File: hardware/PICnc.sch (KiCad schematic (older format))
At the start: 30 parts, among them P1 CONN_13X2, P2 CONN_5X2, P3 CONN_10X2, P4 CONN_8X2, P5 ICSP, P6 CONN_4X2, P7 CONN_2, P8 CONN_2, U1 PIC32MX764F128H, U2 LP2985LV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

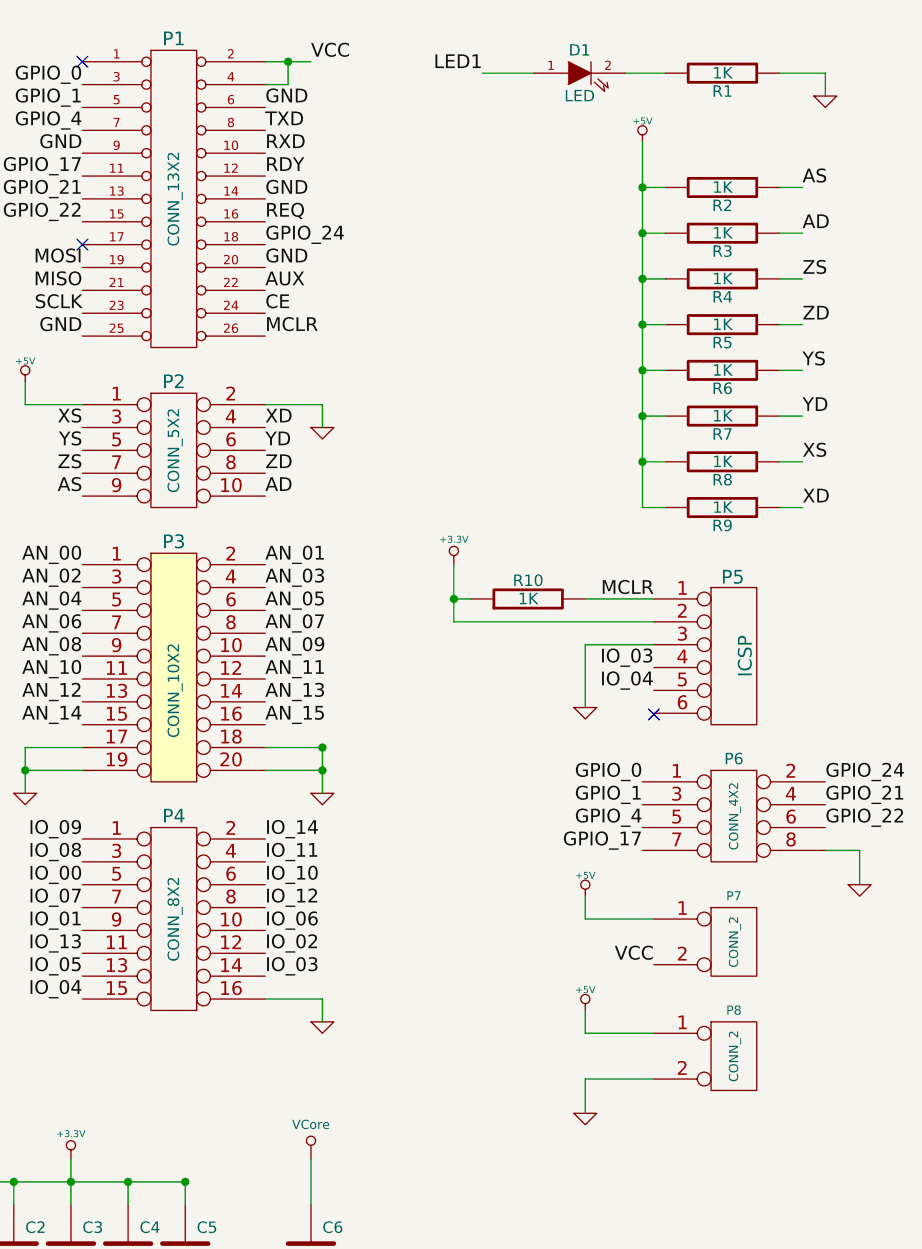
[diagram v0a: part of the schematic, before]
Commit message: minor schematic rename
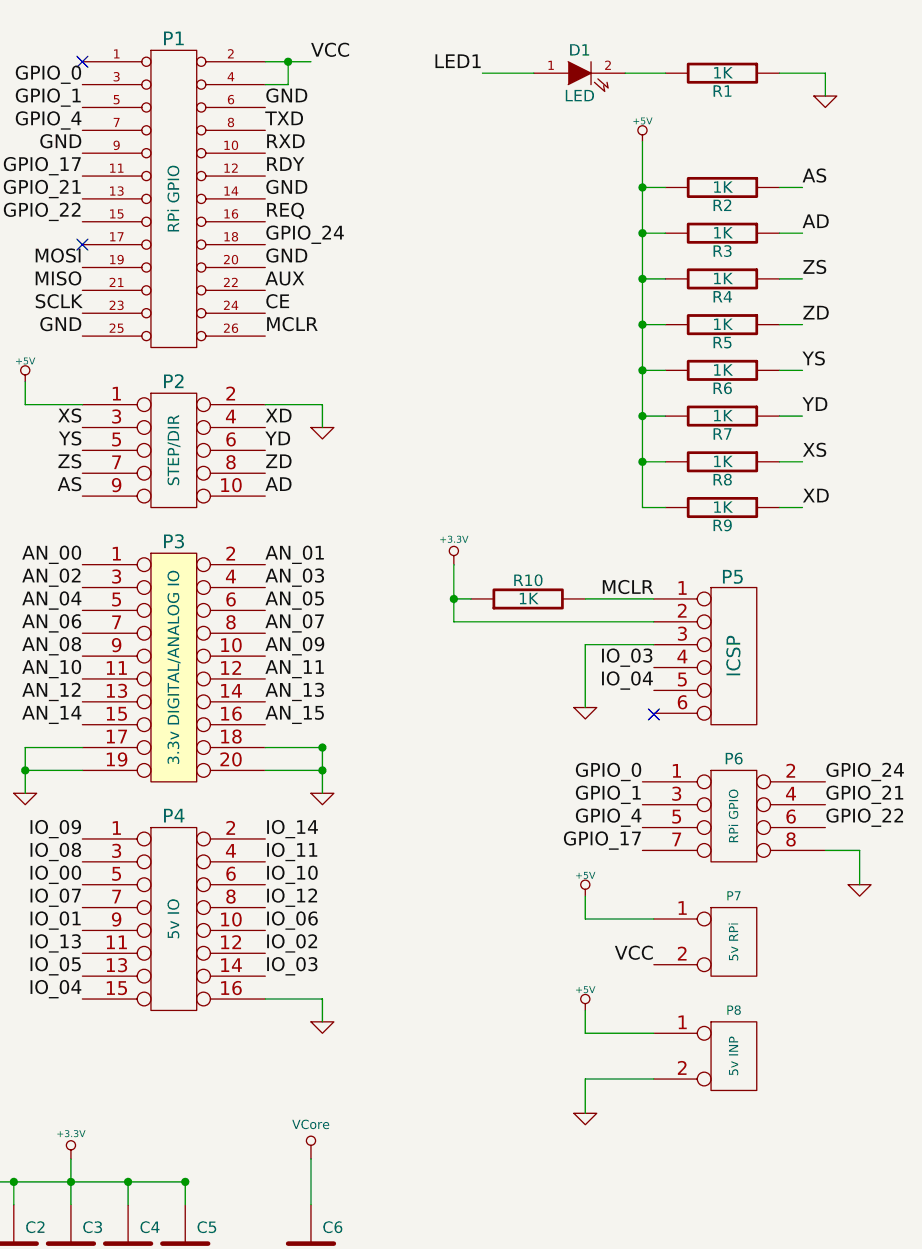
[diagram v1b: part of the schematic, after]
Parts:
- P1: value CONN_13X2 -> RPi GPIO
- P2: value CONN_5X2 -> STEP/DIR
- P3: value CONN_10X2 -> 3.3v DIGITAL/ANALOG IO
- P4: value CONN_8X2 -> 5v IO
- P6: value CONN_4X2 -> RPi GPIO
- P7: value CONN_2 -> 5v RPi
- P8: value CONN_2 -> 5v INP
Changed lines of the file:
@@
-EESchema Schematic File Version 2  date Sunday 17,February,2013 01:55:35 PM SGT
+EESchema Schematic File Version 2  date Monday 18,February,2013 08:21:33 AM SGT
 LIBS:power
 LIBS:device
@@
 Sheet 1 1
 Title "Raspberry Pi PICnc Board"
-Date "17 feb 2013"
+Date "18 feb 2013"
 Rev "A0"
 Comp ""
@@
 	9100 5700 9400 5700
 $Comp
-L GND #PWR?
+L GND #PWR01
 U 1 1 512070BF
 P 9100 5850
-F 0 "#PWR?" H 9100 5850 30  0001 C CNN
+F 0 "#PWR01" H 9100 5850 30  0001 C CNN
 F 1 "GND" H 9100 5780 30  0001 C CNN
 	1    9100 5850
@@
 P 9750 5600
 F 0 "P8" H 9750 5800 40  0000 C CNN
-F 1 "CONN_2" V 9750 5600 40  0000 C CNN
+F 1 "5v INP" V 9750 5600 40  0000 C CNN
 	1    9750 5600
 	1    0    0    -1
 $EndComp
 $Comp
-L +5V #PWR?
+L +5V #PWR02
 U 1 1 512070B4
 P 9100 5400
-F 0 "#PWR?" H 9100 5490 20  0001 C CNN
+F 0 "#PWR02" H 9100 5490 20  0001 C CNN
 F 1 "+5V" H 9100 5490 30  0000 C CNN
 	1    9100 5400
@@
 VCC
 $Comp
-L GND #PWR01
+L GND #PWR03
 U 1 1 512030E4
 P 10300 4850
-F 0 "#PWR01" H 10300 4850 30  0001 C CNN
+F 0 "#PWR03" H 10300 4850 30  0001 C CNN
 F 1 "GND" H 10300 4780 30  0001 C CNN
 	1    10300 4850
@@
 $EndComp
 $Comp
-L +5V #PWR02
+L +5V #PWR04
 U 1 1 512030D0
 P 9100 4900
-F 0 "#PWR02" H 9100 4990 20  0001 C CNN
+F 0 "#PWR04" H 9100 4990 20  0001 C CNN
 F 1 "+5V" H 9100 4990 30  0000 C CNN
 	1    9100 4900
@@
 P 9750 5100
 F 0 "P7" H 9750 5300 40  0000 C CNN
-F 1 "CONN_2" V 9750 5100 40  0000 C CNN
+F 1 "5v RPi" V 9750 5100 40  0000 C CNN
 	1    9750 5100
 	1    0    0    -1
@@
 P 9750 4550
 F 0 "P6" H 9750 4800 50  0000 C CNN
-F 1 "CONN_4X2" V 9750 4550 40  0000 C CNN
+F 1 "RPi GPIO" V 9750 4550 40  0000 C CNN
 	1    9750 4550
 	1    0    0    -1
@@
 P 7300 5000
 F 0 "P4" H 7300 5450 60  0000 C CNN
-F 1 "CONN_8X2" V 7300 5000 50  0000 C CNN
+F 1 "5v IO" V 7300 5000 50  0000 C CNN
 	1    7300 5000
 	1    0    0    -1
@@
 NoConn ~ 6900 1250
 $Comp
-L +5V #PWR03
+L +5V #PWR05
 U 1 1 511F206D
 P 6650 2650
-F 0 "#PWR03" H 6650 2740 20  0001 C CNN
+F 0 "#PWR05" H 6650 2740 20  0001 C CNN
 F 1 "+5V" H 6650 2740 30  0000 C CNN
 	1    6650 2650
@@
 $EndComp
 $Comp
-L GND #PWR04
+L GND #PWR06
 U 1 1 511F201E
 P 7950 2850
-F 0 "#PWR04" H 7950 2850 30  0001 C CNN
+F 0 "#PWR06" H 7950 2850 30  0001 C CNN
 F 1 "GND" H 7950 2780 30  0001 C CNN
 	1    7950 2850
@@
 XS
 $Comp
-L GND #PWR05
+L GND #PWR07
 U 1 1 511F1F5D
 P 6650 4450
-F 0 "#PWR05" H 6650 4450 30  0001 C CNN
+F 0 "#PWR07" H 6650 4450 30  0001 C CNN
 F 1 "GND" H 6650 4380 30  0001 C CNN
 	1    6650 4450
@@
 $EndComp
 $Comp
-L GND #PWR06
+L GND #PWR08
 U 1 1 511F1F45
 P 7950 4450
-F 0 "#PWR06" H 7950 4450 30  0001 C CNN
+F 0 "#PWR08" H 7950 4450 30  0001 C CNN
 F 1 "GND" H 7950 4380 30  0001 C CNN
 	1    7950 4450
@@
 AN_00
 $Comp
-L GND #PWR07
+L GND #PWR09
 U 1 1 511F1238
 P 7950 5450
-F 0 "#PWR07" H 7950 5450 30  0001 C CNN
+F 0 "#PWR09" H 7950 5450 30  0001 C CNN
 F 1 "GND" H 7950 5380 30  0001 C CNN
 	1    7950 5450
@@
 P 7300 3900
 F 0 "P3" H 7300 4450 60  0000 C CNN
-F 1 "CONN_10X2" V 7300 3800 50  0000 C CNN
+F 1 "3.3v DIGITAL/ANALOG IO" V 7300 3900 50  0000 C CNN
 	1    7300 3900
 	1    0    0    -1
@@
 P 7300 2950
 F 0 "P2" H 7300 3250 60  0000 C CNN
-F 1 "CONN_5X2" V 7300 2950 50  0000 C CNN
+F 1 "STEP/DIR" V 7300 2950 50  0000 C CNN
 	1    7300 2950
 	1    0    0    -1
@@
 P 7300 1850
 F 0 "P1" H 7300 2550 60  0000 C CNN
-F 1 "CONN_13X2" V 7300 1850 50  0000 C CNN
+F 1 "RPi GPIO" V 7300 1850 50  0000 C CNN
 	1    7300 1850
 	1    0    0    -1
@@
 P 9750 3850
 F 0 "P5" H 9745 4195 60  0000 C CNN
-F 1 "ICSP" V 9800 3850 60  0000 C CNN
+F 1 "ICSP" V 9750 3850 60  0000 C CNN
 	1    9750 3850
 	1    0    0    -1
@@
 AD
 $Comp
-L +5V #PWR08
+L +5V #PWR010
 U 1 1 5003963F
 P 9350 1600
-F 0 "#PWR08" H 9350 1690 20  0001 C CNN
+F 0 "#PWR010" H 9350 1690 20  0001 C CNN
 F 1 "+5V" H 9350 1690 30  0000 C CNN
 	1    9350 1600
@@
 IO_00
 $Comp
-L +5V #PWR09
+L +5V #PWR011
 U 1 1 5001906A
 P 3625 5750
-F 0 "#PWR09" H 3625 5840 20  0001 C CNN
+F 0 "#PWR011" H 3625 5840 20  0001 C CNN
 F 1 "+5V" H 3625 5840 30  0000 C CNN
 	1    3625 5750
@@
 $EndComp
 $Comp
-L +3.3V #PWR010
+L +3.3V #PWR012
 U 1 1 50018FF2
 P 5650 5750
-F 0 "#PWR010" H 5650 5710 30  0001 C CNN
+F 0 "#PWR012" H 5650 5710 30  0001 C CNN
 F 1 "+3.3V" H 5650 5860 30  0000 C CNN
 	1    5650 5750
@@
 $EndComp
 $Comp
-L GND #PWR011
+L GND #PWR013
 U 1 1 50018FE5
 P 4700 7200
-F 0 "#PWR011" H 4700 7200 30  0001 C CNN
+F 0 "#PWR013" H 4700 7200 30  0001 C CNN
 F 1 "GND" H 4700 7130 30  0001 C CNN
 	1    4700 7200
@@
 MCLR
 $Comp
-L GND #PWR012
+L GND #PWR014
 U 1 1 50018868
 P 9100 4075
-F 0 "#PWR012" H 9100 4075 30  0001 C CNN
+F 0 "#PWR014" H 9100 4075 30  0001 C CNN
 F 1 "GND" H 9100 4005 30  0001 C CNN
 	1    9100 4075
@@
 IO_03
 $Comp
-L +3.3V #PWR013
+L +3.3V #PWR015
 U 1 1 5001876E
 P 8525 3450
-F 0 "#PWR013" H 8525 3410 30  0001 C CNN
+F 0 "#PWR015" H 8525 3410 30  0001 C CNN
 F 1 "+3.3V" H 8525 3560 30  0000 C CNN
 	1    8525 3450
@@
 LED1
 $Comp
-L GND #PWR014
+L GND #PWR016
 U 1 1 500185B5
 P 10150 1400
-F 0 "#PWR014" H 10150 1400 30  0001 C CNN
+F 0 "#PWR016" H 10150 1400 30  0001 C CNN
 F 1 "GND" H 10150 1330 30  0001 C CNN
 	1    10150 1400
@@
 $EndComp
 $Comp
-L +3.3V #PWR015
+L +3.3V #PWR017
 U 1 1 4FF3FE2D
 P 6850 6050
-F 0 "#PWR015" H 6850 6010 30  0001 C CNN
+F 0 "#PWR017" H 6850 6010 30  0001 C CNN
 F 1 "+3.3V" H 6850 6160 30  0000 C CNN
 	1    6850 6050
@@
 $EndComp
 $Comp
-L +3.3V #PWR016
+L +3.3V #PWR018
 U 1 1 4FF3FDD3
 P 3800 1250
-F 0 "#PWR016" H 3800 1210 30  0001 C CNN
+F 0 "#PWR018" H 3800 1210 30  0001 C CNN
 F 1 "+3.3V" H 3800 1360 30  0000 C CNN
 	1    3800 1250
@@
 $EndComp
 $Comp
-L +3.3V #PWR017
+L +3.3V #PWR019
 U 1 1 4FF3FDA2
 P 3400 1250
-F 0 "#PWR017" H 3400 1210 30  0001 C CNN
+F 0 "#PWR019" H 3400 1210 30  0001 C CNN
 F 1 "+3.3V" H 3400 1360 30  0000 C CNN
 	1    3400 1250
@@
 $EndComp
 $Comp
-L GND #PWR018
+L GND #PWR020
 U 1 1 4FF3F882
 P 7900 6850
-F 0 "#PWR018" H 7900 6850 30  0001 C CNN
+F 0 "#PWR020" H 7900 6850 30  0001 C CNN
 F 1 "GND" H 7900 6780 30  0001 C CNN
 	1    7900 6850
@@
 $EndComp
 $Comp
-L GND #PWR019
+L GND #PWR021
 U 1 1 4FF3F72D
 P 6850 6850
-F 0 "#PWR019" H 6850 6850 30  0001 C CNN
+F 0 "#PWR021" H 6850 6850 30  0001 C CNN
 F 1 "GND" H 6850 6780 30  0001 C CNN
 	1    6850 6850
@@
 $EndComp
 $Comp
-L GND #PWR020
+L GND #PWR022
 U 1 1 4FE5BF24
 P 3650 5350
-F 0 "#PWR020" H 3650 5350 30  0001 C CNN
+F 0 "#PWR022" H 3650 5350 30  0001 C CNN
 F 1 "GND" H 3650 5280 30  0001 C CNN
 	1    3650 5350
@@
 OSC1
 $Comp
-L GND #PWR021
+L GND #PWR023
 U 1 1 4FE5BC91
 P 2650 6900
-F 0 "#PWR021" H 2650 6900 30  0001 C CNN
+F 0 "#PWR023" H 2650 6900 30  0001 C CNN
 F 1 "GND" H 2650 6830 30  0001 C CNN
 	1    2650 6900
